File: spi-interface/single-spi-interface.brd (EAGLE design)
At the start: 39.6 x 39.6 mm, 92 parts, among them Q1 AO3402, Q2 AO3402, U1 LY3200, U2 LY3200, U3 LY3200, U4 ADXL335

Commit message: SPI interface cleanup.
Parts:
- removed TP3, TP4, TP7, TP8: (no value), jonnew:TESTPOINT_SMALL
- added R12, R13, R14: 100, jonnew:0201
- moved ANT2 0.51 mm to (-34.7, -55.6), flipped to the bottom
- flipped ANT1 to the bottom
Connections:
- net CS+: now also R12.2
- net CS-: now also R12.1
- net GND: now also C1.1, C24.1; no longer C1.2, C24.2, TP7.1, TP8.1
- net MOSI+: now also R14.2
- net MOSI-: now also R14.1
- net SCLK+: now also R13.2
- net SCLK-: now also R13.1
- net VCC: now also C1.2, C24.2; no longer C1.1, C24.1, TP3.1, TP4.1
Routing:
- net GND: track 10.1 -> 8.19 mm, vias 3 -> 2
- net VCC: track 1.75 -> 0.00 mm, vias 1 -> 0

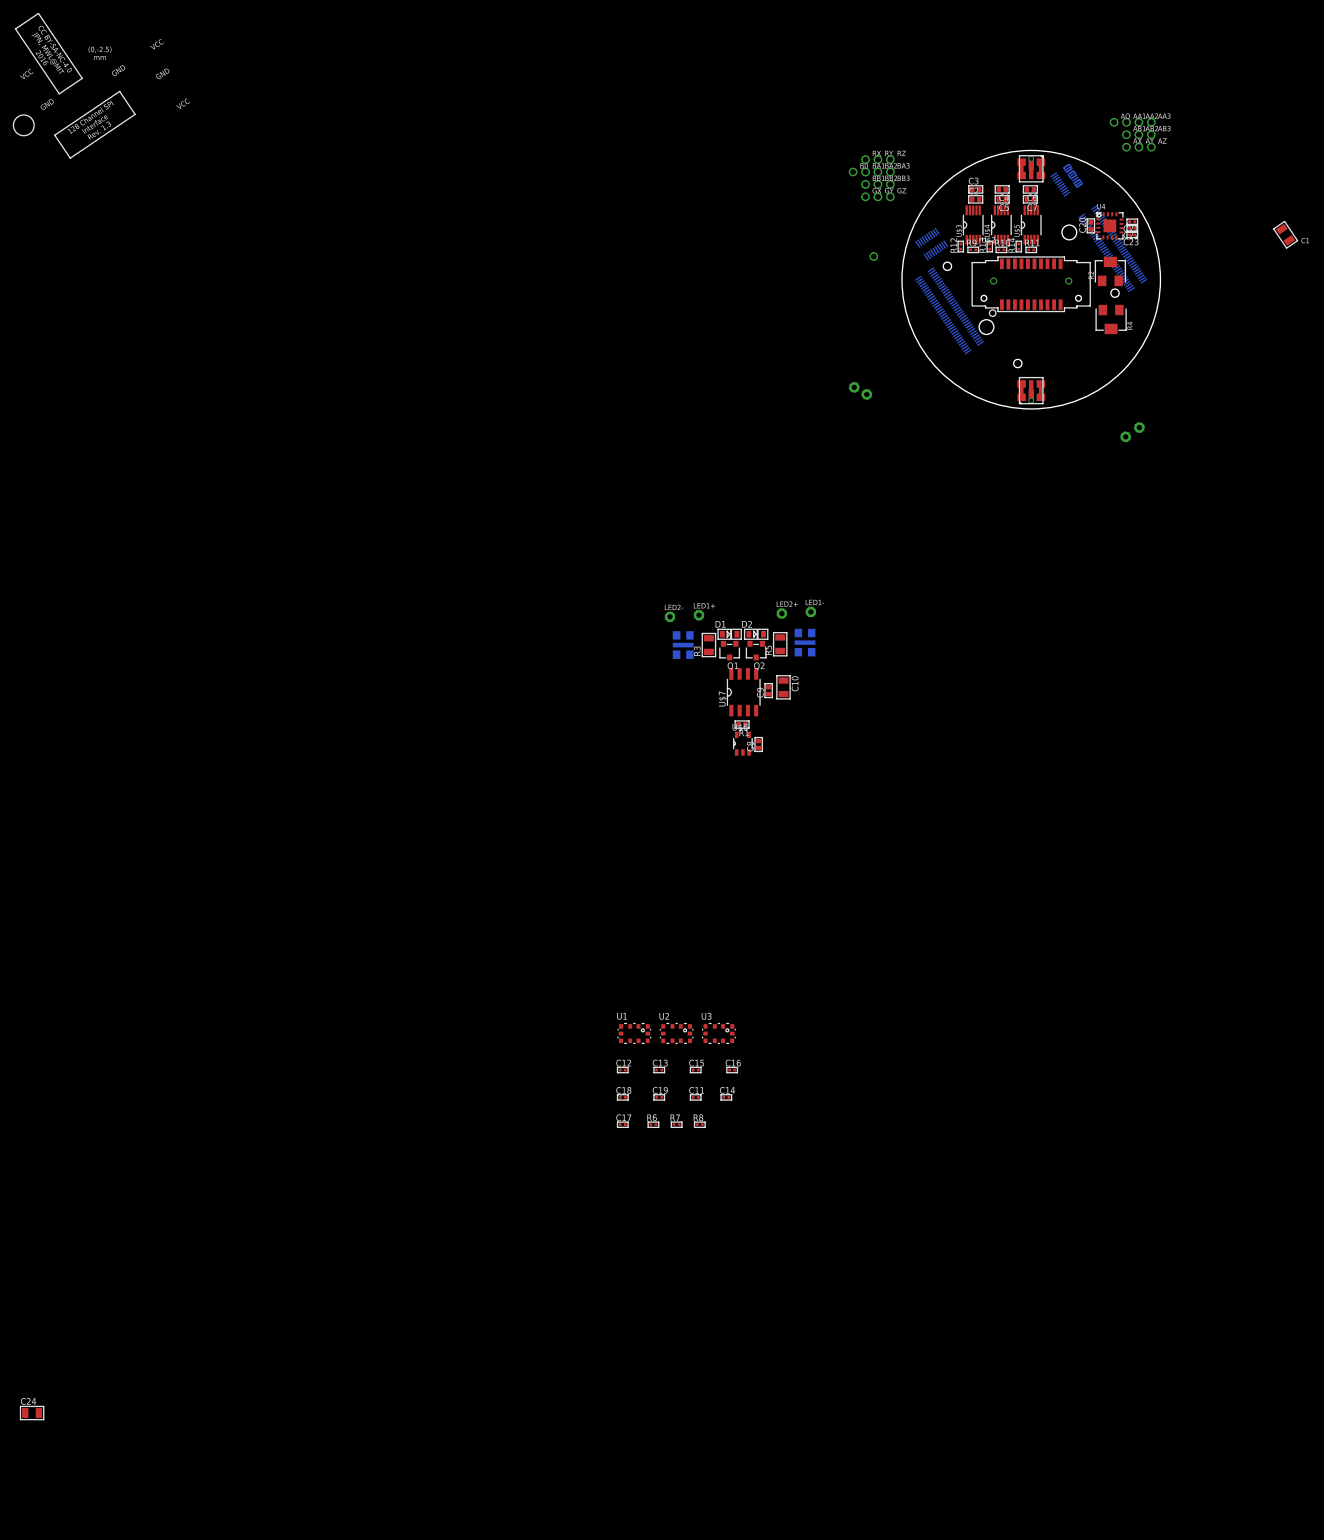
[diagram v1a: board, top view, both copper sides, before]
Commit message: Made spice model of on-headstage LED stim circuit.
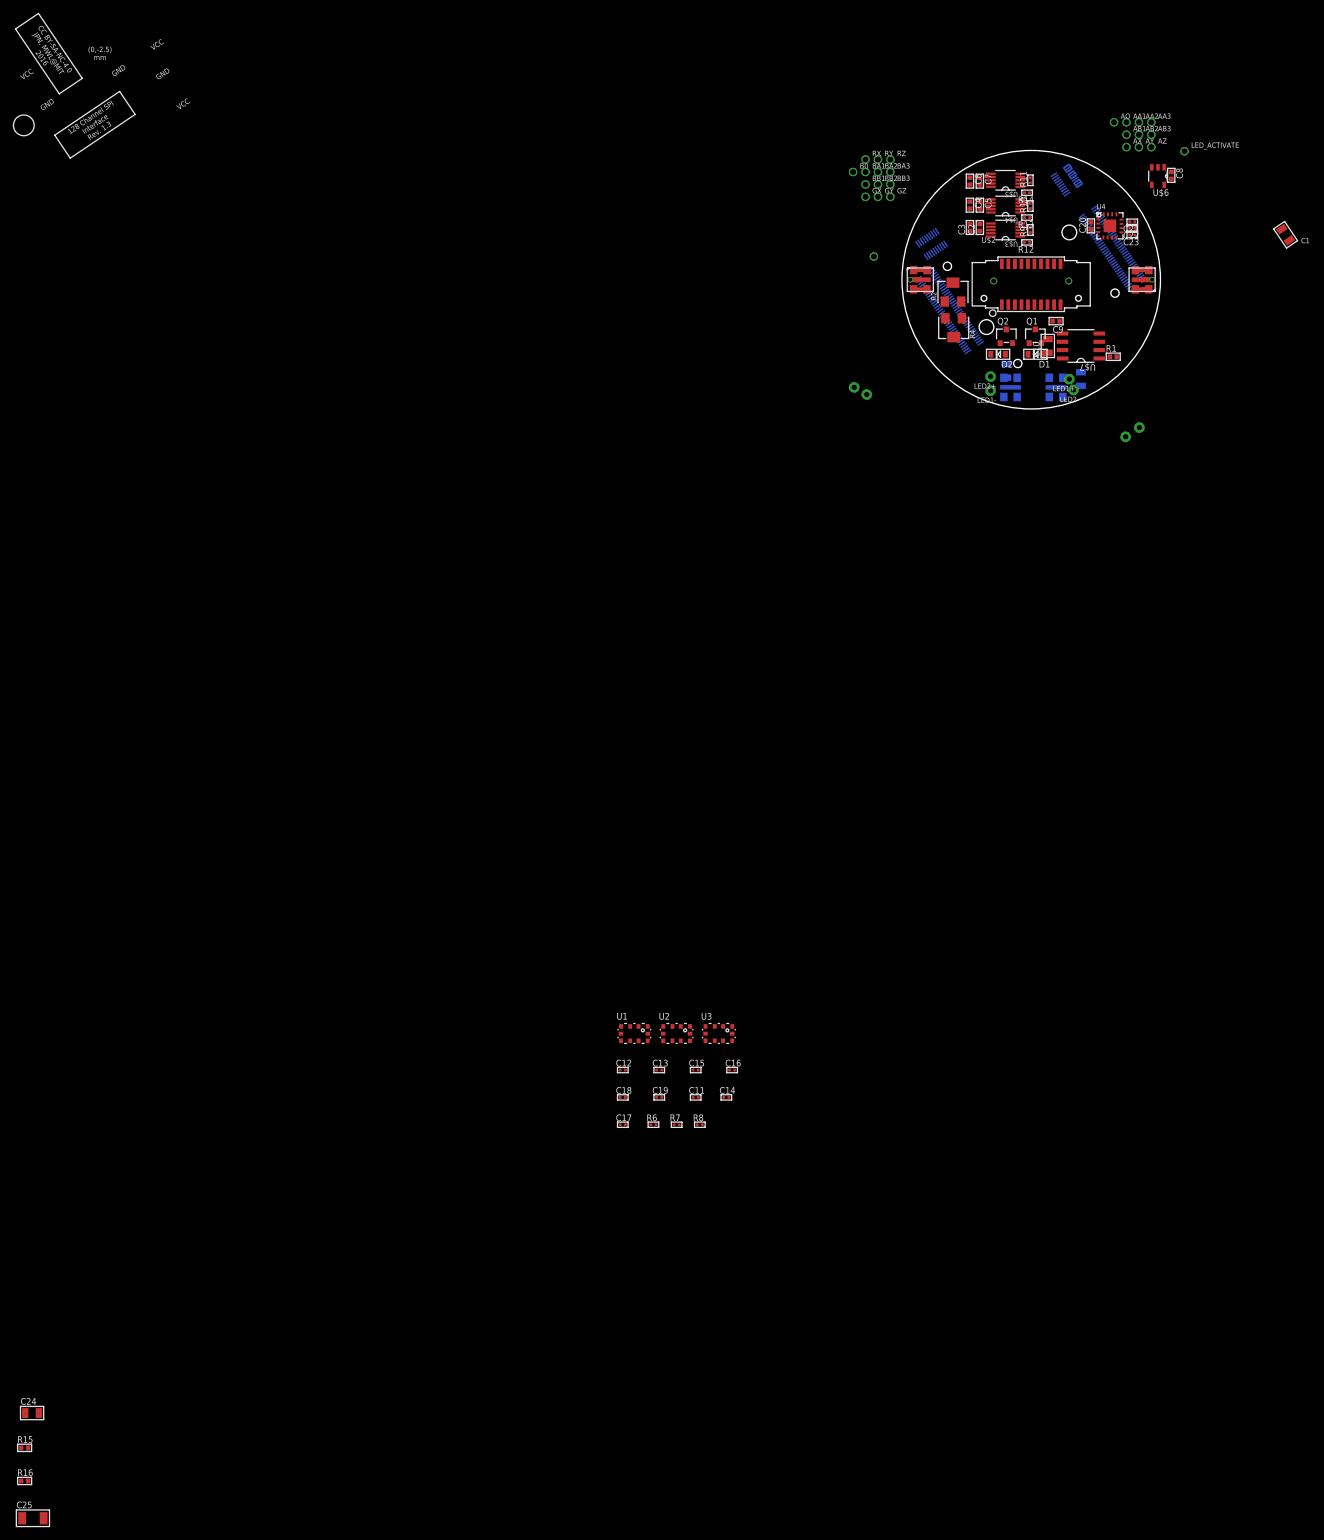
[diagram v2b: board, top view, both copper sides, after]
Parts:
- added C25: 47uF, jonnew:1206
- added LED_ACTIVATE: (no value), jonnew:TESTPOINT_0.035IN
- added R15, R16: 10, jonnew:0402
- moved U$6 107.8 mm to (19.4, 15.9), turned to 180 degrees
- moved C8 107.8 mm to (21.5, 16.0), turned to 270 degrees
- moved R1 80.1 mm to (12.6, -11.8), turned to 0 degrees
- moved U$7 74.1 mm to (7.62, -10.2), turned to 180 degrees
- moved C9 71.8 mm to (3.81, -6.35), turned to 180 degrees
- moved LED2- 71.0 mm to (6.48, -16.9), turned to 180 degrees
- moved R3 70.1 mm to (7.62, -15.2), flipped to the bottom
- moved ANT1 69.5 mm to (3.81, -16.5), turned to 270 degrees
- moved Q1 68.7 mm to (0.64, -7.62), turned to 0 degrees
- moved LED1+ 67.3 mm to (5.84, -15.2), turned to 180 degrees
- moved C10 66.2 mm to (2.54, -10.2), turned to 90 degrees
- moved D1 63.6 mm to (0.64, -11.4), turned to 180 degrees
- moved Q2 63.2 mm to (-3.81, -7.62), turned to 0 degrees
- moved D2 56.7 mm to (-5.08, -11.4), turned to 180 degrees
- moved R5 54.4 mm to (-3.81, -14.0), flipped to the bottom, turned to 270 degrees
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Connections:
- new net N$20: D1.C, Q1.G, R15.2
- new net N$22: R15.1, R16.1, U$7.6, U$7.7
- net N$5: now also LED_ACTIVATE.1
- net N$7: now also R16.2; no longer D1.C, Q1.G, U$7.6, U$7.7
- net VDD: now also C25.1
- net VSS: now also C25.2
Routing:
- added copper zone on layer 2, net LED-

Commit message: More SPI interface layout.
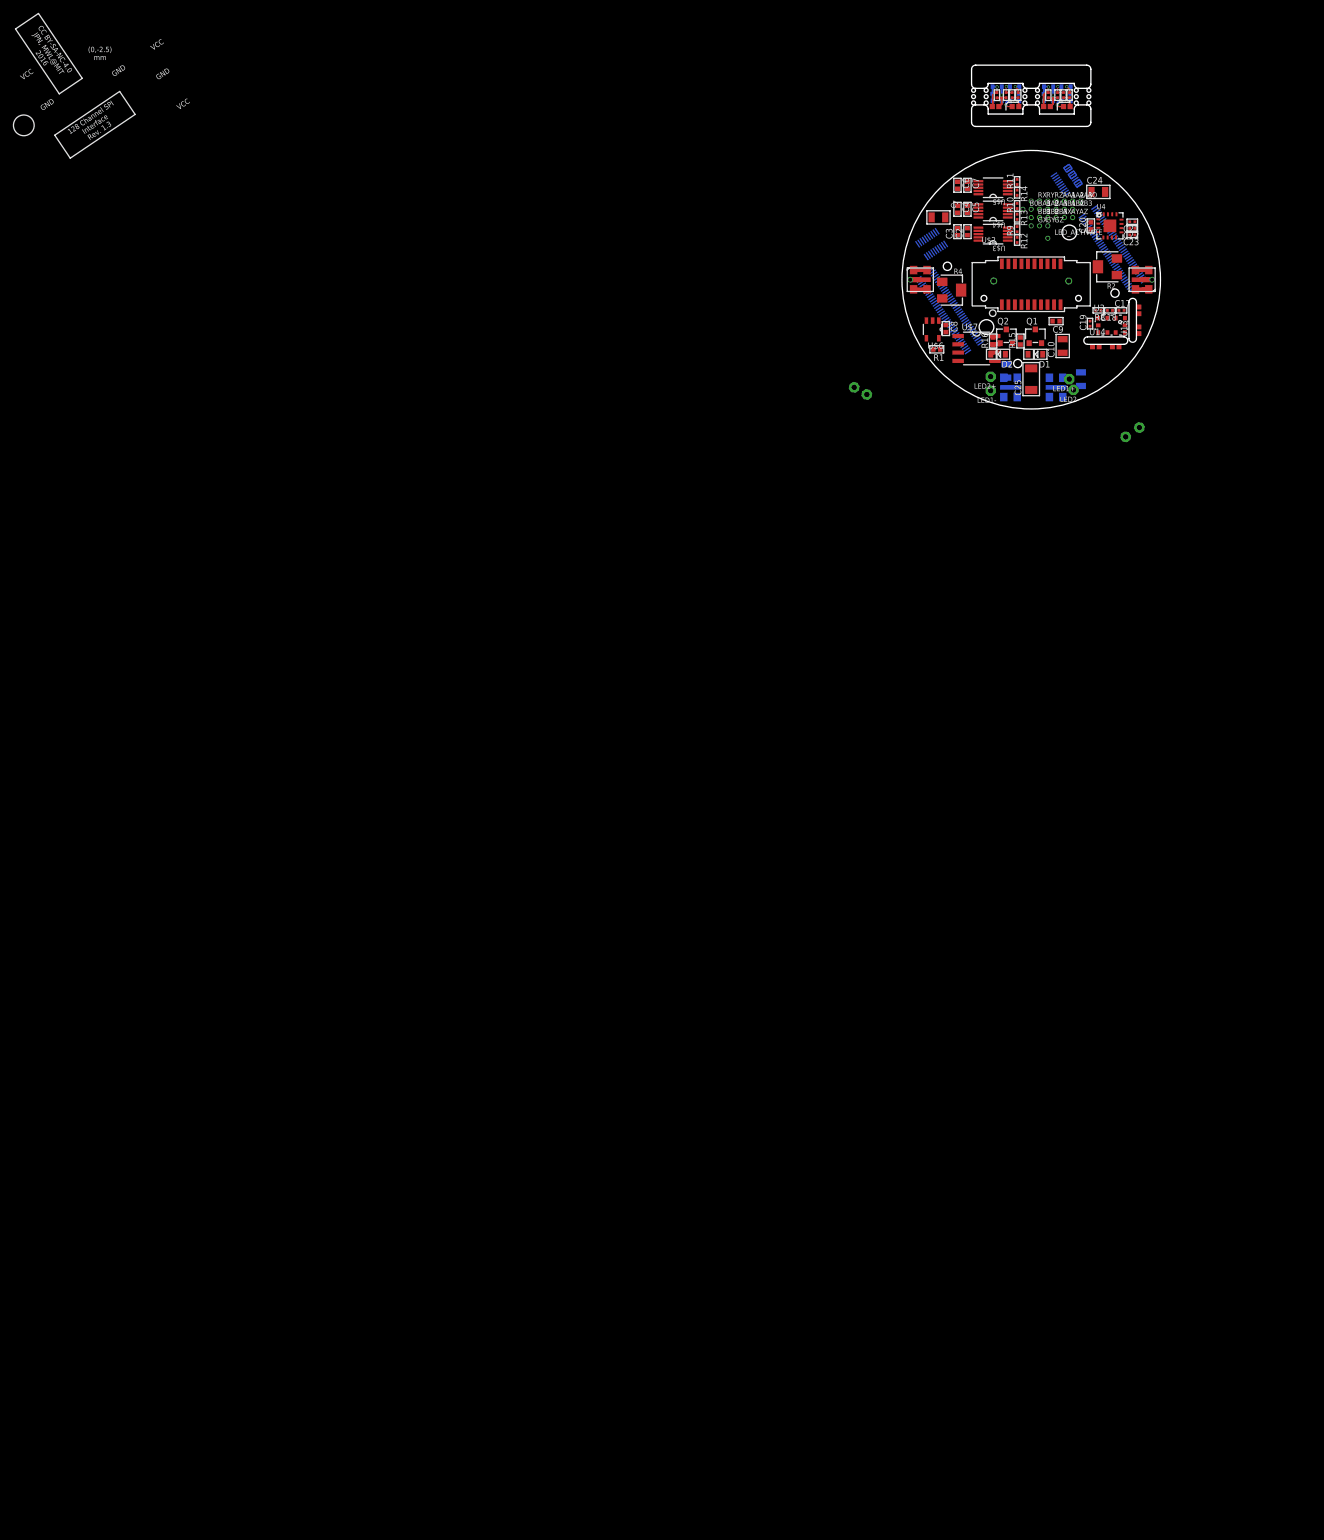
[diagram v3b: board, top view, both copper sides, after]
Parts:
- added TP10, TP11, TP12, TP3, TP4, TP7, TP8, TP9: (no value), jonnew:TP08SQ
- added U13, U14: (no value), jonnew:LY3200-VERT-MODULE
- AA1, AA2, AA3, AB1, AB2, AB3, AO, AX, AY, AZ, B0, BA1, BA2, BA3, BB1, BB2, BB3, GX, GY, GZ, LED_ACTIVATE, RX, RY, RZ: device jonnew:TESTPOINT_0.035IN -> jonnew:TESTPOINT_0.5MM
- moved C24 248.5 mm to (10.3, 13.5)
- moved C25 232.2 mm to (0.00, -15.2), turned to 90 degrees
- moved R16 229.3 mm to (-5.84, -9.40), turned to 90 degrees
- moved R15 228.2 mm to (-1.65, -9.40), turned to 90 degrees
- moved R7 168.9 mm to (5.88, 28.3), turned to 90 degrees
- moved R6 167.5 mm to (-1.99, 28.3), turned to 90 degrees
- moved C14 161.8 mm to (4.03, 28.3), turned to 270 degrees
- moved C12 160.9 mm to (-2.92, 28.3), turned to 270 degrees
- moved C11 160.9 mm to (-3.85, 28.3), turned to 270 degrees
- moved C15 159.7 mm to (4.96, 28.3), turned to 270 degrees
- moved C13 158.2 mm to (-5.26, 28.3), turned to 270 degrees
- moved C16 157.1 mm to (2.62, 28.3), turned to 270 degrees
- moved U2 155.4 mm to (4.00, 28.5), flipped to the bottom
- moved U1 154.9 mm to (-3.87, 28.5), flipped to the bottom
- moved C17 146.4 mm to (13.8, -4.70)
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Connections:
- net OUT2 renamed OUTZ
- net VREF2 renamed VREFZ
- removed net OUT: GX.1, U1.6
- removed net OUT1: GY.1, U2.6
- removed net VREF: RX.1, U1.7
- removed net VREF1: RY.1, U2.7
- new net OUTX: GX.1, U14.OUT
- new net OUTY: GY.1, U13.OUT
- new net OUT_GX: TP4.TP, U1.6
- new net OUT_GY: TP10.TP, U2.6
- new net REFX: RX.1, U14.REF
- new net REFY: RY.1, U13.REF
- new net VREF_GX: TP8.TP, U1.7
- new net VREF_GY: TP12.TP, U2.7
- net GND: now also TP11.TP, TP7.TP, U13.GND, U14.GND
- net VCC: now also TP3.TP, TP9.TP, U13.VCC, U14.VCC
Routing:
- net GND: track 8.19 -> 25.2 mm, vias 2 -> 6
- net VCC: track 0.00 -> 13.2 mm, vias 0 -> 2
- net N$2: track 0.00 -> 2.42 mm, vias 0 -> 1
- net N$10: track 0.00 -> 2.42 mm, vias 0 -> 1
- net VREF_GX: track 0.00 -> 2.17 mm, vias 0 -> 1
- net VREF_GY: track 0.00 -> 2.17 mm, vias 0 -> 1
- net OUT_GX: track 0.00 -> 1.95 mm, vias 0 -> 1
- net OUT_GY: track 0.00 -> 1.80 mm, vias 0 -> 1
- net N$8: track 0.00 -> 0.93 mm
- net N$14: track 0.00 -> 0.93 mm
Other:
- board size 39.6 x 39.6 mm -> 39.6 x 52.7 mm

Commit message: SPI interface layout progress.
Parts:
- removed ANT1, ANT2: MLE-V01, jonnew:LED-MLE
- added LED1, LED2: MLE-V01, jonnew:LED-MLE
- C2, C4, C6: device jonnew:0402 -> jonnew:0201
- moved AA1 17.7 mm to (16.5, 24.4)
- moved AA2 17.7 mm to (17.8, 24.4)
- moved AA3 17.7 mm to (19.1, 24.4)
- moved AB1 17.7 mm to (16.5, 23.1)
- moved AB2 17.7 mm to (17.8, 23.1)
- moved AB3 17.7 mm to (19.1, 23.1)
- moved AO 17.7 mm to (20.3, 24.4)
- moved AX 17.7 mm to (16.5, 21.8)
- moved AY 17.7 mm to (17.8, 21.8)
- moved AZ 17.7 mm to (19.1, 21.8)
- moved B0 17.7 mm to (11.4, 23.1)
- moved BA1 17.7 mm to (12.7, 23.1)
- moved BA2 17.7 mm to (14.0, 23.1)
- moved BA3 17.7 mm to (15.2, 23.1)
- moved BB1 17.7 mm to (12.7, 21.8)
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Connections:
- net N$12: now also LED2.A1, LED2.A2; no longer ANT2.A1, ANT2.A2
- net N$3: now also LED1.A1, LED1.A2; no longer ANT1.A1, ANT1.A2
- net VSS: now also LED1.C1, LED1.C2, LED1.HS, LED2.C1, LED2.C2, LED2.HS; no longer ANT1.C1, ANT1.C2, ANT1.HS, ANT2.C1, ANT2.C2, ANT2.HS
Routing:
- net N$22: track 0.00 -> 26.4 mm
- net CS+_HSA: track 0.00 -> 21.0 mm, vias 0 -> 1
- net CS-_HSA: track 0.00 -> 20.9 mm, vias 0 -> 1
- net SCLK+_HSA: track 0.00 -> 20.9 mm, vias 0 -> 1
- net SCLK-_HSA: track 0.00 -> 20.3 mm, vias 0 -> 1
- net MOSI-_HSB: track 0.00 -> 17.5 mm, vias 0 -> 1
- net MOSI+_HSA: track 0.00 -> 15.3 mm
- net MOSI-: track 0.00 -> 15.2 mm
- net MOSI-_HSA: track 0.00 -> 15.1 mm
- net MOSI+_HSB: track 0.00 -> 14.9 mm, vias 0 -> 1
- net MOSI+: track 0.00 -> 14.1 mm
- net SCLK-_HSB: track 0.00 -> 14.1 mm, vias 0 -> 1
- net CS-_HSB: track 0.00 -> 12.3 mm, vias 0 -> 1
- net SCLK+_HSB: track 0.00 -> 12.2 mm, vias 0 -> 1
- net SCLK-: track 0.00 -> 10.5 mm
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
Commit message: More SPI interface routing.
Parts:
- removed C10: 10uF, jonnew:0805
- moved C25 8.32 mm to (-4.32, -9.40), turned to 270 degrees
- moved C9 5.03 mm to (-6.86, -13.8), turned to 0 degrees
- moved C24 4.69 mm to (6.22, 15.8), turned to 304 degrees
- moved R15 2.34 mm to (-1.02, -10.7)
- moved R3 2.18 mm to (-1.78, -17.3)
- moved R16 2.01 mm to (3.17, -10.8)
- moved U13 1.73 mm to (15.3, -7.75)
- moved U14 1.73 mm to (10.6, -11.4)
- moved R5 1.53 mm to (2.16, -17.1), turned to 180 degrees
- moved LED2- 1.42 mm to (7.75, -16.5)
- moved C17 1.34 mm to (12.7, -5.40)
- moved R8 1.34 mm to (9.14, -5.40)
- moved U3 1.34 mm to (11.2, -7.68)
- moved C19 1.34 mm to (7.87, -7.43)
- moved C18 1.34 mm to (10.9, -5.40)
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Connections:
- net VDD: no longer C10.1
- net VSS: no longer C10.2
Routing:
- net MISO2-: track 0.00 -> 28.4 mm, vias 0 -> 1
- net MISO1-: track 0.00 -> 27.6 mm, vias 0 -> 1
- net MISO2+: track 0.00 -> 27.0 mm, vias 0 -> 1
- net MISO1+: track 0.00 -> 26.5 mm, vias 0 -> 1
- net N$22: track 26.4 -> 1.27 mm
- net MISO4-: track 0.00 -> 13.2 mm
- net MISO4+: track 0.00 -> 11.2 mm
- net N$4: track 10.3 -> 0.00 mm
- net N$11: track 10.1 -> 0.00 mm
- net MISO3+: track 0.00 -> 9.47 mm
- net MISO3-: track 0.00 -> 8.87 mm
- net N$20: track 6.72 -> 0.00 mm
- net N$7: track 6.08 -> 0.00 mm
- net VCC: vias 9 -> 10
- net GND: vias 16 -> 19
- added copper zone on layer 15, net VDD
- added copper zone on layer 2, net VSS
- removed copper zone on layer 2, net LED-
